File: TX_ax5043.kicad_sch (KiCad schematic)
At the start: 27 parts, among them P6 CONUFL001-SMD-T, P7 CONUFL001-SMD-T, Q7 DMP2037U-7, U23 AX5043

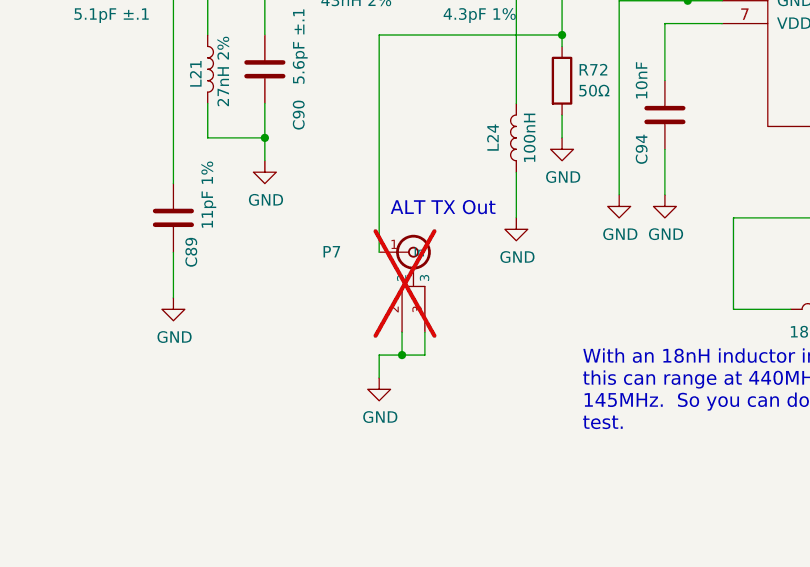
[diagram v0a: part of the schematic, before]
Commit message: Move the power LED to a better location
Not right in the middle of things, put it on the edge.

Signed-off-by: Corey Minyard <corey@minyard.net>
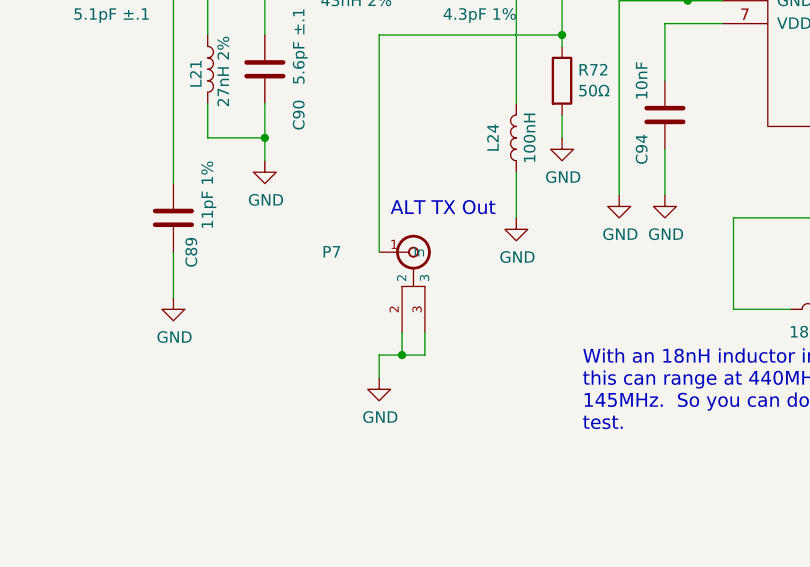
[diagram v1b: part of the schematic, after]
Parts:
- P7: now fitted; now in the parts list
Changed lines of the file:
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@@
 		(unit 1)
 		(exclude_from_sim no)
-		(in_bom no)
+		(in_bom yes)
 		(on_board yes)
-		(dnp yes)
+		(dnp no)
 		(property "Reference" "P7"
 			(at 196.85 170.18 0)

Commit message: More minor tweaks and cleanups
Signed-off-by: Corey Minyard <corey@minyard.net>
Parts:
- P7: now not fitted; now left out of the parts list
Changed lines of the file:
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@@
 		(unit 1)
 		(exclude_from_sim no)
-		(in_bom yes)
+		(in_bom no)
 		(on_board yes)
-		(dnp no)
+		(dnp yes)
 		(property "Reference" "P7"
 			(at 196.85 170.18 0)
